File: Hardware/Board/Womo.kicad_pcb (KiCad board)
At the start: 4 copper layers, 255 x 150 mm, 465 parts, among them IC1 SPSGRFC-868, IC200 BTS6143D, IC201 BTS6143D, IC203 BTS6143D, IC204 BTS6143D, J1 USB_B_Micro, J2 Conn_ARM_JTAG_SWD_20, J3 SD_Card, J300 734-264, J301 733-368, J302 733-368, J303 733-368, J304 Truma, J305 Dormetic, J306 733-366, J307 733-366, J308 733-366, J309 733-366, J310 733-370, J311 734-163, J312 734-163, J313 734-163, J314 734-163, J315 734-168, J316 733-363, J317 RJ45_Shielded, J318 Spare, J319 SENSOR, J320 Raspberry_Pi_2_3, J321 Wasser, J322 Abwasser, J323 733-370, J324 Waveshare IoT Hat, J325 734-168, J326 733-366, J400 USB_B_Micro, J401 RJ45_Shielded, J500 SENSOR, K300 5-1393243-2, K301 5-1393243-2, K302 5-1393243-2, K303 5-1393243-2, Q100 2N7002, Q102 2N7002, Q103 2N7002, Q104 2N7002, Q200 2N7002, Q201 2N7002, Q202 2N7002, Q203 2N7002, SW1 Boot, SW3 Reset, U1 STM32L476ZGTx, U100 MAX17572, U101 MAX17572, U102 MAX17572, U104 MAX17574, U105 MAX17574, U2 M25Q128A, U200 SN74LV4052A, U201 TJA1029T, U202 TJA1029T, U203 TJA1029T, U204 TJA1029T, U205 SN74LV4052A, U206 SN74LV4052A, U207 MAX3072E, U208 MAX3072E, U209 MAX3072E, U210 MAX3072E, U211 MAX11615, U212 PCF8574A, U213 TJA1049T-3, U214 DS2482S-800+, U215 SN74LV4052A, U216 Si8642BB-B-IS1, U217 Si8642BB-B-IS1, U3 24AA02UID, U300 max4896atp+, U301 max4896atp+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

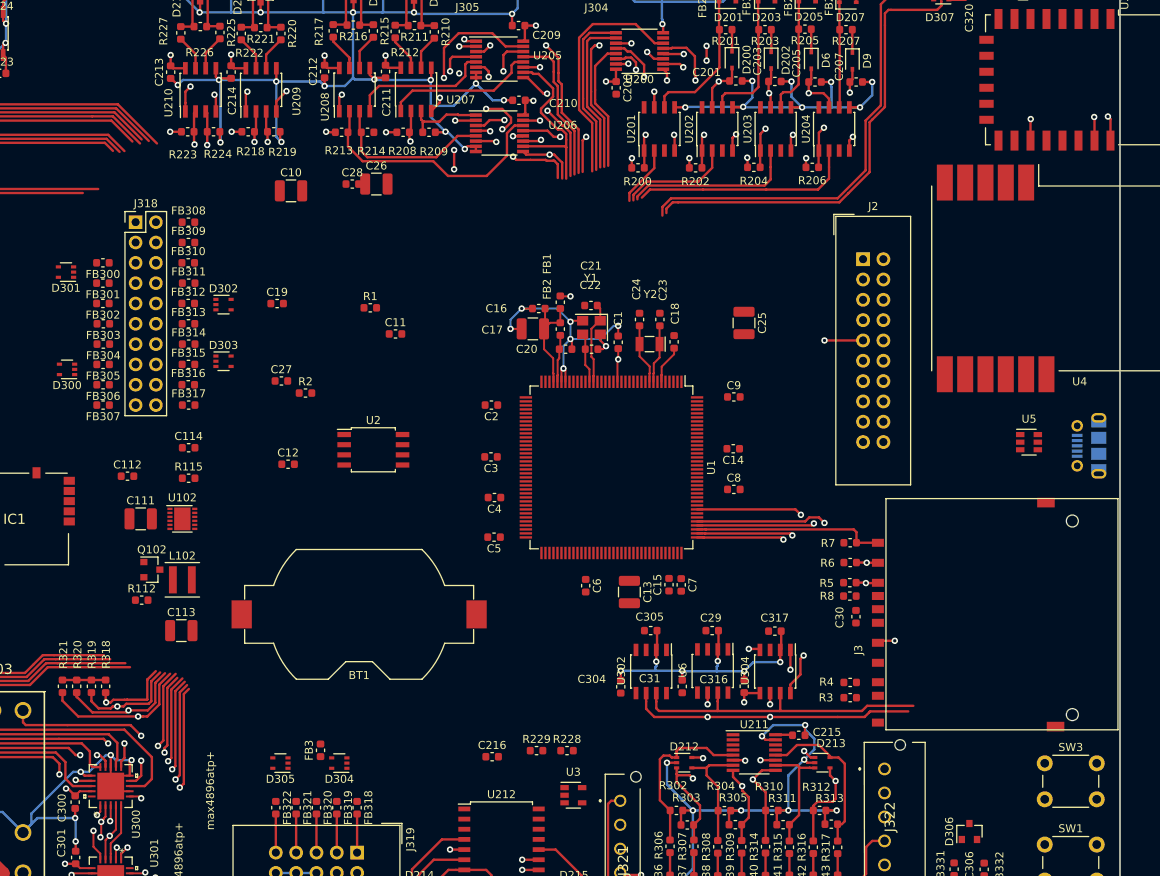
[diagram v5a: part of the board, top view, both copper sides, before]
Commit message: Rechte Seite CPU gerouted, SPI 1 / 2 getauscht.
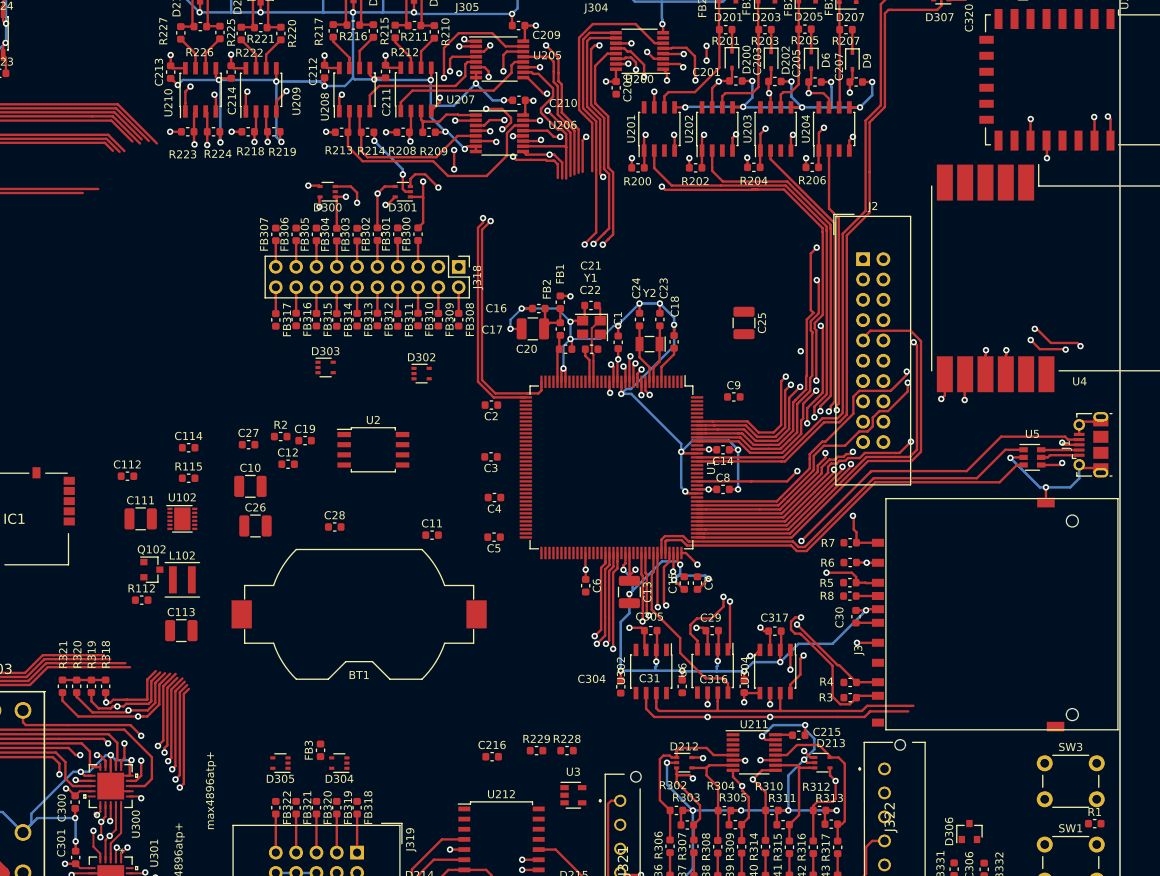
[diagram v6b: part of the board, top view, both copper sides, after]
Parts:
- J1: moved to F.Cu
- moved R1 111.2 mm to (386.8, 246.6)
- moved C26 45.3 mm to (281.9, 209.4)
- moved D301 43.3 mm to (300.4, 167.6)
- moved C28 42.9 mm to (291.8, 209.6)
- moved J318 40.8 mm to (307.3, 177.0), turned to 270 degrees
- moved FB300 39.6 mm to (302.3, 172.9), turned to 90 degrees
- moved D300 39.4 mm to (291.0, 167.6)
- moved FB301 37.4 mm to (299.7, 172.9), turned to 90 degrees
- moved C10 37.3 mm to (281.3, 204.5)
- moved FB308 35.9 mm to (307.3, 183.6), turned to 270 degrees
- moved FB302 35.4 mm to (297.2, 172.9), turned to 90 degrees
- moved FB303 33.6 mm to (294.6, 173.0), turned to 90 degrees
- moved FB309 32.7 mm to (304.8, 183.6), turned to 270 degrees
- moved FB304 32.2 mm to (292.1, 173.0), turned to 90 degrees
- moved FB305 31.2 mm to (289.6, 173.0), turned to 90 degrees
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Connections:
- IC1 pad 10: SPI2_NSS -> SPI1_NSS
- IC1 pad 7: SPI2_SCK -> SPI1_SCK
- IC1 pad 8: SPI2_MISO -> SPI1_MISO
- IC1 pad 9: SPI2_MOSI -> SPI1_MOSI
- U4 pad 6: SPI1_SCK -> SPI2_SCK
- U4 pad 7: SPI1_NSS -> SPI2_NSS
- U4 pad 8: SPI1_MOSI -> SPI2_MOSI
- U4 pad 9: SPI1_MISO -> SPI2_MISO
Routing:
- net GND: track 1119.4 -> 1265.0 mm, vias 116 -> 133
- net Boot0: track 0.00 -> 119.6 mm, vias 0 -> 3
- net SLP-LIN1: track 7.58 -> 116.0 mm, vias 0 -> 2
- net RESET: track 0.00 -> 97.5 mm, vias 0 -> 3
- net SLP-LIN2: track 14.1 -> 111.5 mm, vias 0 -> 2
- net SLP-LIN3: track 21.5 -> 103.0 mm, vias 0 -> 2
- net ESP_Boot: track 0.00 -> 78.8 mm, vias 0 -> 2
- net LIN_SEL_A0: track 20.2 -> 97.3 mm, vias 0 -> 4
- net USB_ID: track 0.00 -> 73.6 mm, vias 0 -> 2
- net SLP-LIN4: track 27.9 -> 100.7 mm, vias 0 -> 2
- net JTAG_TMS: track 0.00 -> 65.2 mm, vias 0 -> 3
- net PF6: track 0.00 -> 63.5 mm, vias 0 -> 2
- net PF7: track 0.00 -> 63.1 mm, vias 0 -> 2
- net PF4: track 0.00 -> 62.5 mm, vias 0 -> 2
- net USART1_RX_CTRL: track 0.00 -> 62.3 mm, vias 0 -> 2
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
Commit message: CPU Layout, Fehlerkorrektur
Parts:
- moved U2 6.54 mm to (302.3, 203.3), turned to 90 degrees
- moved C9 1.28 mm to (340.5, 193.4)
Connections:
- U1 pad 70: LPUART_RX_RX485 -> LPUART_RX_RS485
- U205 pad 3: LPUART3_TX_RS485 -> LPUART_TX_RS485
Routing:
- net LPUART_TX_RS485: track 0.00 -> 142.7 mm, vias 0 -> 3
- net ESP_Enable: track 0.00 -> 133.5 mm, vias 0 -> 4
- net ESP_Reset: track 0.00 -> 131.1 mm, vias 0 -> 4
- net RE_RS485: track 12.8 -> 131.4 mm, vias 2 -> 4
- net LIN_SEL_EN: track 29.6 -> 148.1 mm, vias 0 -> 2
- net LPUART_RTS_DE_RS485: track 19.1 -> 134.1 mm, vias 2 -> 4
- net LPUART_RX_RS485: track 19.3 -> 133.3 mm, vias 0 -> 1
- net RS485_SEL_A0: track 23.5 -> 133.0 mm, vias 0 -> 2
- net LIN_SEL_A1: track 36.1 -> 141.9 mm, vias 1 -> 2
- net RS485_SEL_EN: track 24.2 -> 127.3 mm, vias 3 -> 5
- net RS485_SEL_A1: track 19.8 -> 122.9 mm, vias 2 -> 4
- net GND: track 1265.0 -> 1296.7 mm, vias 133 -> 137
- net LPUART3_TX_RS485: track 26.7 -> 0.00 mm, vias 2 -> 0
- net +3V3: track 134.4 -> 147.5 mm, vias 13 -> 14
- net I2C2_SDA: track 98.4 -> 108.5 mm
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
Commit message: CPU Routing komplett
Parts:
- moved C113 134.2 mm to (155.3, 157.3)
- moved Q102 121.7 mm to (162.8, 155.3)
- moved L102 119.3 mm to (168.0, 159.1)
- moved C111 115.8 mm to (162.4, 160.2)
- moved R112 110.1 mm to (173.4, 161.9)
- moved U102 104.6 mm to (177.5, 165.3)
- moved C19 104.3 mm to (380.8, 246.6)
- moved C112 104.2 mm to (168.8, 165.6)
- moved C114 99.2 mm to (178.8, 170.4)
- moved R115 98.6 mm to (181.9, 167.3)
- moved C26 98.5 mm to (367.9, 161.2)
- moved D221 89.9 mm to (159.5, 234.4)
- moved D222 80.9 mm to (159.6, 229.3)
- moved C25 67.7 mm to (280.0, 208.8), turned to 0 degrees
- moved C136 62.8 mm to (167.8, 207.1)
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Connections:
- D303 pad 5: I2C1SCL -> I2C1_SCL
- D304 pad 1: INt_2_XL -> INT_MAG_DRDY
- D304 pad 3: INT_MAG_DRDY -> INt_2_XL
- FB317 pad 2: I2C1SCL -> I2C1_SCL
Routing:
- net +BATT: track 49.5 -> 655.6 mm, vias 5 -> 6
- net GND: track 1296.7 -> 1870.1 mm, vias 137 -> 172
- net +3.3VA: track 397.6 -> 822.6 mm, vias 30 -> 47
- net +3V3: track 147.5 -> 521.6 mm, vias 14 -> 25
- net I2C3_SDA: track 0.00 -> 217.7 mm, vias 0 -> 7
- net I2C3_SCL: track 0.00 -> 213.8 mm, vias 0 -> 7
- net I2C2_SCL: track 109.2 -> 297.1 mm, vias 0 -> 6
- net Rasp_Shutdown: track 0.00 -> 187.5 mm, vias 0 -> 1
- net Rasp_down: track 0.00 -> 186.4 mm, vias 0 -> 1
- net I2C2_SDA: track 108.5 -> 291.7 mm, vias 0 -> 5
- net IO_INT: track 0.00 -> 169.0 mm, vias 0 -> 6
- net INT_1_XL: track 0.00 -> 166.2 mm, vias 0 -> 4
- net INT_MAG_DRDY: track 0.00 -> 163.8 mm, vias 0 -> 4
- net INt_2_XL: track 0.00 -> 162.5 mm, vias 0 -> 4
- net RASPI_TX_CTRL: track 0.00 -> 158.9 mm, vias 0 -> 3
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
